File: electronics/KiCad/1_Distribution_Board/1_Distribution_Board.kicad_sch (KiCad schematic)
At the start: 10 parts, among them Q1 DMG2305UX, SW1 SW_Push

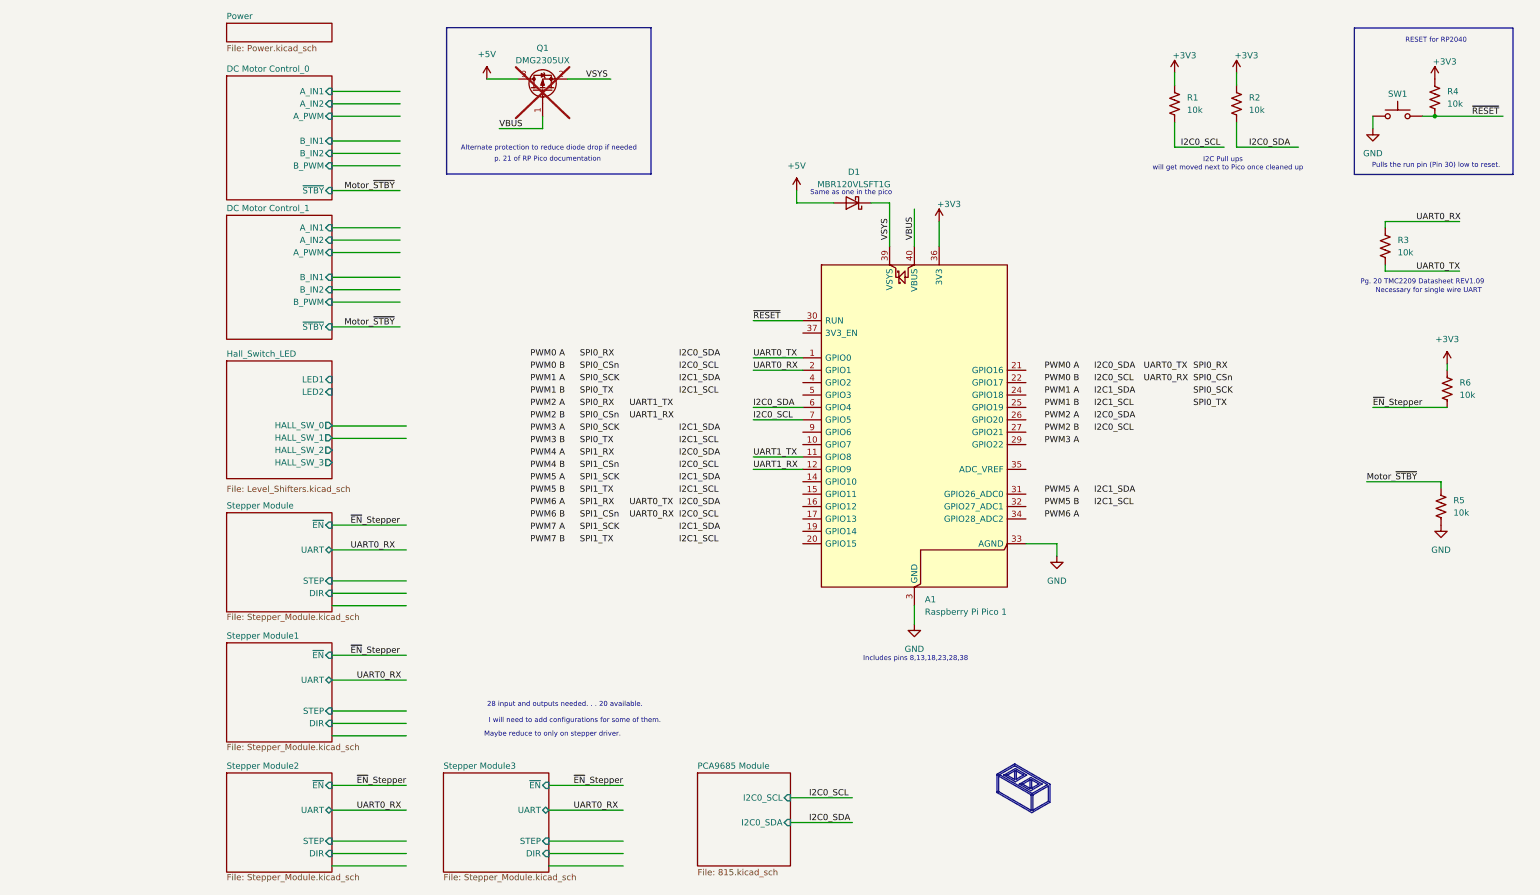
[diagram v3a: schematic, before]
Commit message: Pin Mapping for Steppers
Updated SCH and PCB for pin mapping of Stepper Drivers. Also established naming convention for processor pin labels.
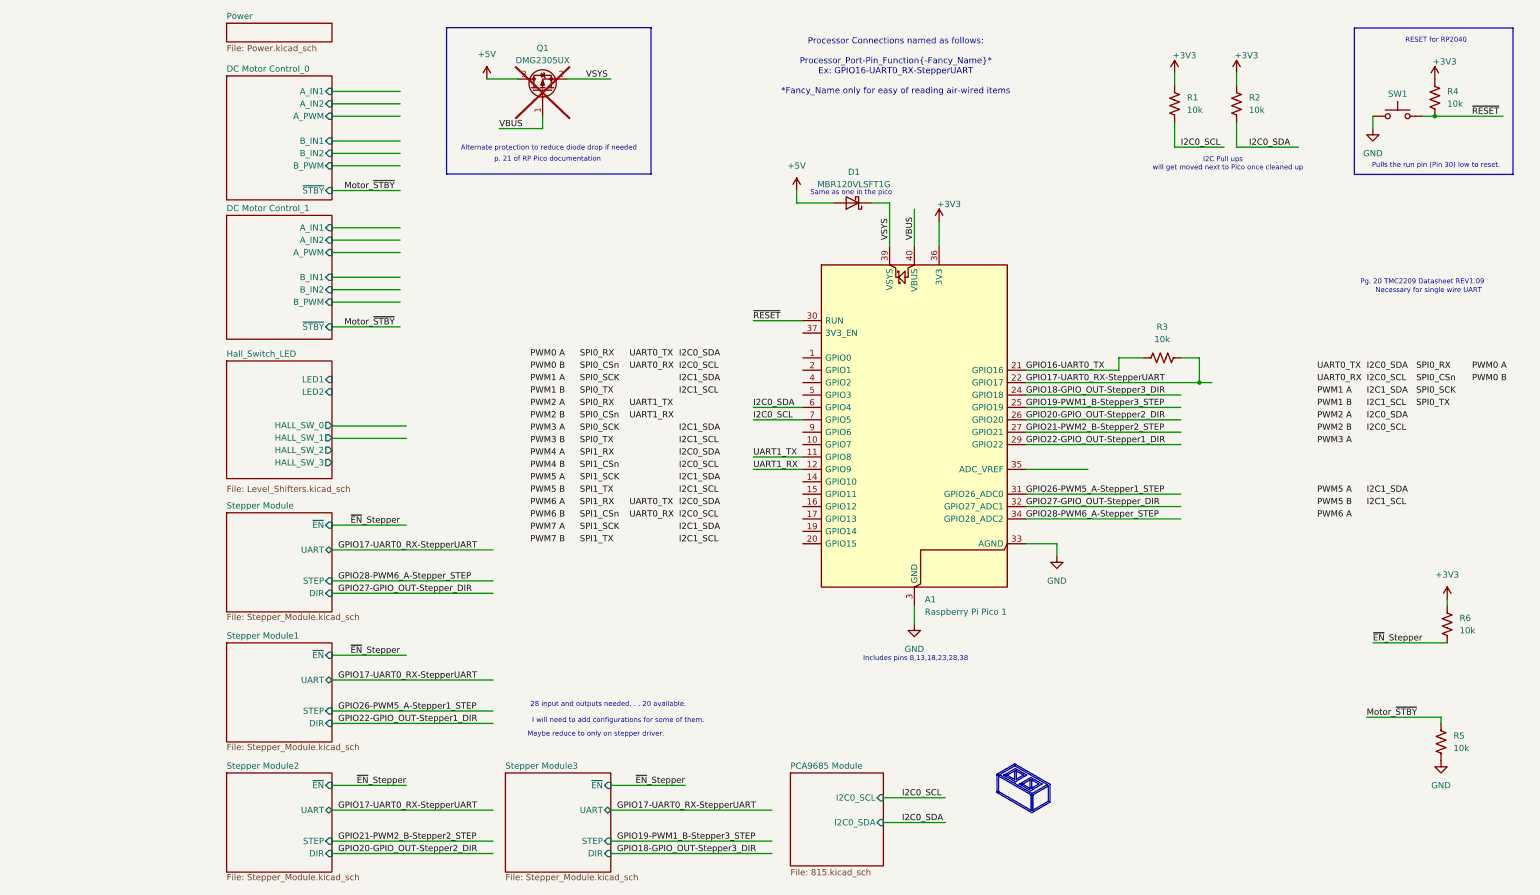
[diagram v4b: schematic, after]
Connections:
- net UART0_RX: no longer A1.2 (GPIO1), R3.1
- net UART0_TX: no longer A1.1 (GPIO0), R3.2
- net GPIO16-UART0_TX: now reaches A1.21 (GPIO16)
- net GPIO16-UART0_TX: now also R3.1
- net GPIO17-UART0_RX-StepperUART: now reaches A1.22 (GPIO17)
- net GPIO17-UART0_RX-StepperUART: now also R3.2
- net GPIO18-GPIO_OUT-Stepper3_DIR: now reaches A1.24 (GPIO18)
- net GPIO19-PWM1_B-Stepper3_STEP: now reaches A1.25 (GPIO19)
- net GPIO20-GPIO_OUT-Stepper2_DIR: now reaches A1.26 (GPIO20)
- net GPIO21-PWM2_B-Stepper2_STEP: now reaches A1.27 (GPIO21)
- net GPIO22-GPIO_OUT-Stepper1_DIR: now reaches A1.29 (GPIO22)
- net GPIO26-PWM5_A-Stepper1_STEP: now reaches A1.31 (GPIO26_ADC0)
- net GPIO27-GPIO_OUT-Stepper_DIR: now reaches A1.32 (GPIO27_ADC1)
- net GPIO28-PWM6_A-Stepper_STEP: now reaches A1.34 (GPIO28_ADC2)
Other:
- note added: "Processor Connections named as follows: Processor_Port-Pin_Function{-Fancy_Name}* Ex: GPIO16-UART0_RX-StepperUART *Fancy_Name only for easy of reading air-wired items"
- moved on the sheet: R3, R5, R6

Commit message: Full Layout V0.1 Distributor
Full layout of distributor complete and ready for review. SCH updated but needs main page cleaned up.
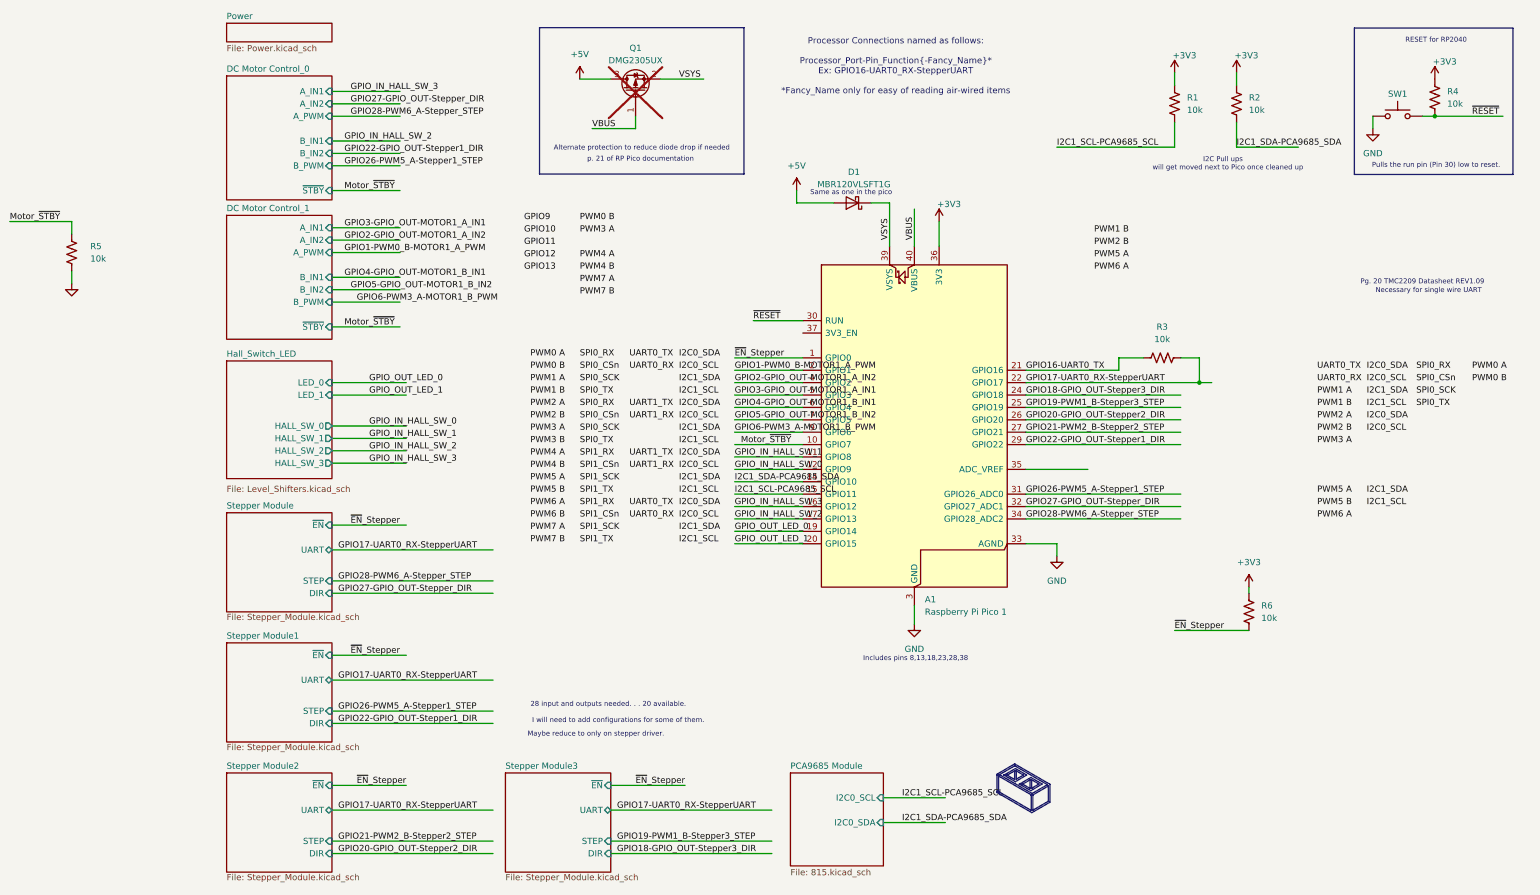
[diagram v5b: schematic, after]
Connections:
- net I2C0_SCL: no longer A1.7 (GPIO5), R1.2
- net I2C0_SDA: no longer A1.6 (GPIO4), R2.2
- net Motor_~{STBY}: now also A1.10 (GPIO7)
- net UART1_RX: no longer A1.12 (GPIO9)
- net UART1_TX: no longer A1.11 (GPIO8)
- net ~{EN}_Stepper: now also A1.1 (GPIO0)
- net I2C1_SDA-PCA9685_SDA: now reaches A1.14 (GPIO10)
- net I2C1_SDA-PCA9685_SDA: now also R2.2
- net I2C1_SCL-PCA9685_SCL: now reaches A1.15 (GPIO11)
- net I2C1_SCL-PCA9685_SCL: now also R1.2
- net GPIO_IN_HALL_SW_3: now reaches A1.16 (GPIO12)
- net GPIO_IN_HALL_SW_2: now reaches A1.17 (GPIO13)
- net GPIO_OUT_LED_0: now reaches A1.19 (GPIO14)
- net GPIO1-PWM0_B-MOTOR1_A_PWM: now reaches A1.2 (GPIO1)
- net GPIO_OUT_LED_1: now reaches A1.20 (GPIO15)
- net GPIO2-GPIO_OUT-MOTOR1_A_IN2: now reaches A1.4 (GPIO2)
- net GPIO3-GPIO_OUT-MOTOR1_A_IN1: now reaches A1.5 (GPIO3)
- net GPIO6-PWM3_A-MOTOR1_B_PWM: now reaches A1.9 (GPIO6)
- new net GPIO4-GPIO_OUT-MOTOR1_B_IN1: A1.6 (GPIO4)
- new net GPIO5-GPIO_OUT-MOTOR1_B_IN2: A1.7 (GPIO5)
- new net GPIO_IN_HALL_SW_0: A1.12 (GPIO9)
- new net GPIO_IN_HALL_SW_1: A1.11 (GPIO8)
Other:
- sheet Hall_Switch_LED ports: added LED_0, LED_1; removed LED1, LED2
- moved on the sheet: Q1, R5, R6

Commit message: SCH Cleanup for review
Cleaned up Processor page and cleaned up all other pages with notes for clarity
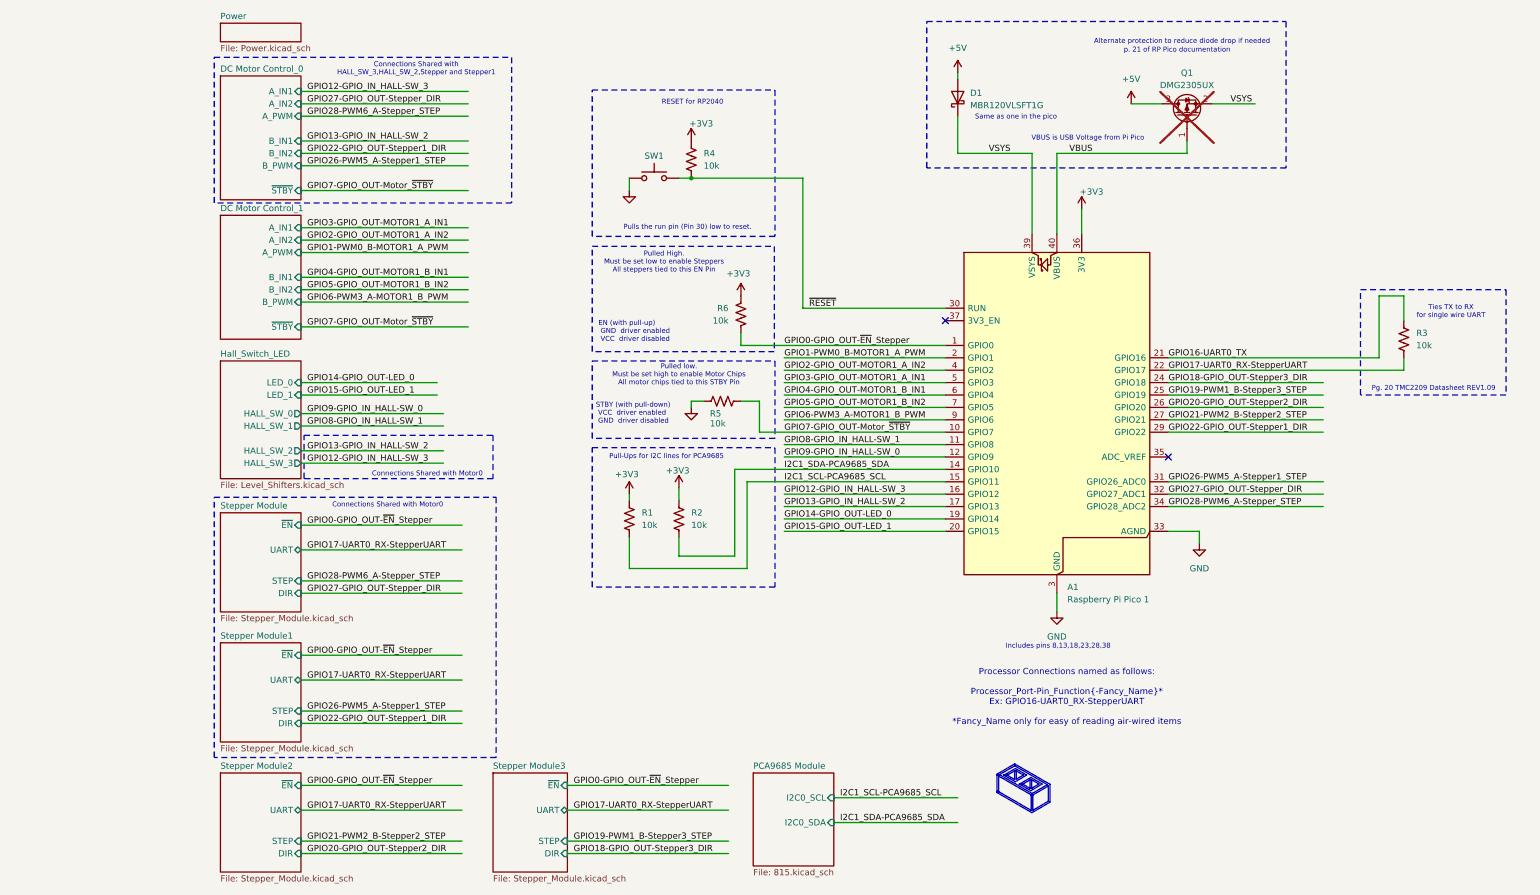
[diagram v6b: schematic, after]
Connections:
- net GPIO_IN_HALL_SW_0 renamed GPIO9-GPIO_IN_HALL-SW_0
- net GPIO_IN_HALL_SW_1 renamed GPIO8-GPIO_IN_HALL-SW_1
- net GPIO_IN_HALL_SW_2 renamed GPIO13-GPIO_IN_HALL-SW_2
- net GPIO_IN_HALL_SW_3 renamed GPIO12-GPIO_IN_HALL-SW_3
- net GPIO_OUT_LED_0 renamed GPIO14-GPIO_OUT-LED_0
- net GPIO_OUT_LED_1 renamed GPIO15-GPIO_OUT-LED_1
- net Motor_~{STBY} renamed GPIO7-GPIO_OUT-Motor_~{STBY}
- net ~{EN}_Stepper renamed GPIO0-GPIO_OUT-~{EN}_Stepper
- no-connect marks 0 -> 2
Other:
- note added: "Connections Shared with HALL_SW_3,HALL_SW_2,Stepper and Stepper1"
- note added: "Connections Shared with Motor0"
- note added: "EN (with pull-up) GND driver enabled VCC driver disabled"
- note added: "Pull-Ups for I2C lines for PCA9685"
- note added: "Pulled High. Must be set low to enable Steppers All steppers tied to this EN Pin"
- note added: "Pulled low. Must be set high to enable Motor Chips All motor chips tied to this STBY Pin"
- note added: "STBY (with pull-down) VCC driver enabled GND driver disabled"
- note added: "Ties TX to RX for single wire UART"
- note added: "VBUS is USB Voltage from Pi Pico"
- note removed: "28 input and outputs needed. . . 20 available."
- note removed: "I will need to add configurations for some of them."
- note removed: "I2C Pull ups"
- note removed: "Maybe reduce to only on stepper driver."
- note removed: "Necessary for single wire UART"
- note removed: "will get moved next to Pico once cleaned up"
- moved on the sheet: A1, D1, Q1, R1, R2, R3, R4, R5, R6, SW1

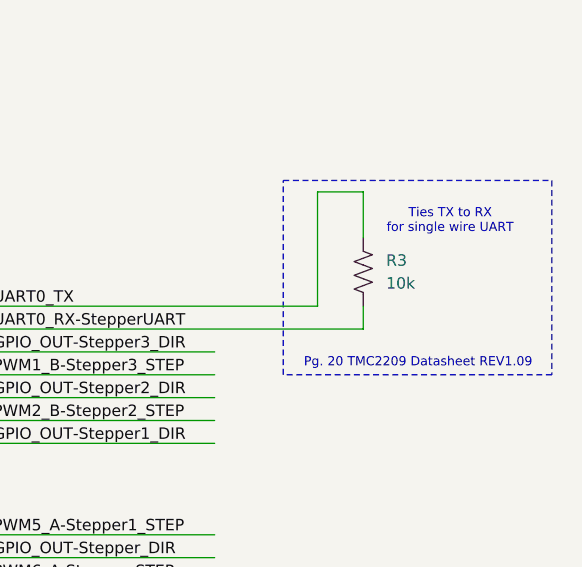
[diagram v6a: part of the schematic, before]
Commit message: Updates based on final review
Updated silk and R3 Value. Cleaned up minor traces for style. This version is ready for JLCPCB quote request.
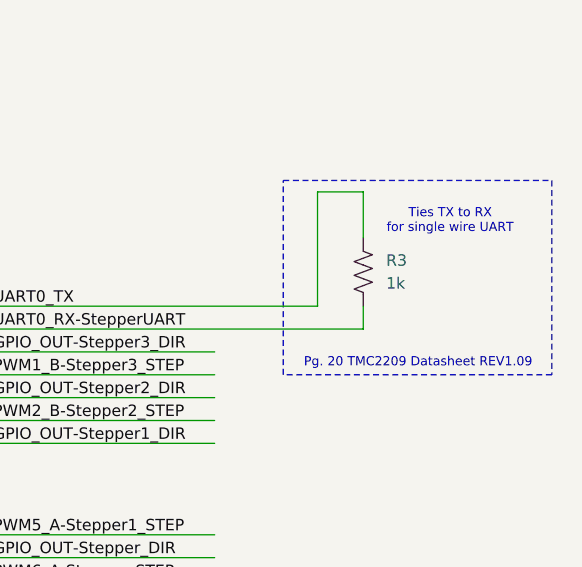
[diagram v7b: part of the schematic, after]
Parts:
- R3: value 10k -> 1k
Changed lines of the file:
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@@
 			)
 		)
-		(property "Value" "10k"
+		(property "Value" "1k"
 			(at 264.16 81.2799 0)
 			(effects
